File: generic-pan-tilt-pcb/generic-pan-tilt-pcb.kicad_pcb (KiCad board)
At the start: 2 copper layers, 85 x 50 mm, 89 parts, among them J1 B4P-VH-FB-B, J10 USB4115-03-C, J11 Conn_01x08, J12 Conn_01x08, J13 Conn_01x05, J2 NC5MAV, J3 NC5FAV, J4 Conn_01x03, J5 BM03B-SRSS-TB, J6 Conn_01x03, J7 BM03B-SRSS-TB, J8 B12B-PH-SM4-TB, J9 B12B-PH-SM4-TB, SW1 PTS 647 SK70 SMTR2 LFS, SW2 PTS 647 SK70 SMTR2 LFS, SW3 219-12LPST, U1 RP2040, U2 W25Q128JVS, U3 AP63203WU, U4 ISO1450DW, U5 MCP23017_SO, U6 LIS3DH, Y1 ABM8-272-T3

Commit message: layout progress
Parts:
- moved C28 194.8 mm to (162.2, 110.5)
- moved C14 192.4 mm to (158.9, 116.7), turned to 90 degrees
- moved C23 192.0 mm to (120.0, 121.0), turned to 90 degrees
- moved C26 189.2 mm to (128.0, 116.3), turned to -90 degrees
- moved C16 185.4 mm to (153.9, 116.7), turned to 90 degrees
- moved C25 182.6 mm to (125.3, 107.0), turned to 0 degrees
- moved C27 180.3 mm to (125.3, 108.5), turned to 0 degrees
- moved R15 177.6 mm to (183.8, 112.2)
- moved R16 177.6 mm to (183.8, 114.8)
- moved R17 177.6 mm to (183.8, 117.3)
- moved C15 176.2 mm to (159.0, 87.8), turned to 0 degrees
- moved C24 174.7 mm to (122.5, 95.5), turned to -90 degrees
- moved C13 174.6 mm to (156.0, 85.2), turned to 90 degrees
- moved C11 173.4 mm to (159.8, 93.0), turned to 0 degrees
- moved C7 173.4 mm to (150.7, 98.5), turned to -90 degrees
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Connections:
- net Net-(PS1-+Vout) renamed /generic-pan-tilt-pcb_rs485/+3V3_ISO_UNFILTERED
- net Net-(U1-USB_DM) renamed /generic-pan-tilt-pcb_rp2040/USB_UNTERMINATED_D+
- net Net-(U1-USB_DP) renamed /generic-pan-tilt-pcb_rp2040/USB_UNTERMINATED_D-
- net Net-(U3-BST) renamed /generic-pan-tilt-pcb_24v_to_3.3v/+3V3_BST
- net Net-(U3-SW) renamed /generic-pan-tilt-pcb_24v_to_3.3v/+3V3_UNFILTERED
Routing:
- net +3V3: track 0.00 -> 269.7 mm, vias 0 -> 6
- net +24V: track 0.00 -> 103.6 mm
- net /I2C_MOT_SCL: track 0.00 -> 65.5 mm, vias 0 -> 3
- net /I2C_MOT_SDA: track 0.00 -> 65.3 mm, vias 0 -> 3
- net /SPI_MOT_PICO: track 0.00 -> 60.1 mm, vias 0 -> 4
- net /SPI_MOT_POCI: track 0.00 -> 58.2 mm, vias 0 -> 3
- net /SPI_MOT_CS_MOT0_GPIO: track 0.00 -> 58.0 mm, vias 0 -> 2
- net /RS485_B-: track 0.00 -> 57.5 mm
- net /SPI_MOT_SCK: track 0.00 -> 57.0 mm, vias 0 -> 3
- net /SPI_MOT_CS_MOT0_CNTLR: track 0.00 -> 53.9 mm, vias 0 -> 2
- net GND: track 0.00 -> 53.8 mm, vias 0 -> 10
- net /RS485_A+: track 0.00 -> 45.5 mm, vias 0 -> 1
- net /generic-pan-tilt-pcb_dmx-expansion/EXP_IN_+: track 0.00 -> 35.7 mm
- net +1V1: track 0.00 -> 33.6 mm, vias 0 -> 3
- net /RS485_OUT_B-: track 0.00 -> 32.0 mm
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- added copper zone on B.Cu, net /RS485_GND
- added copper zone on F.Cu, net /RS485_GND
- added copper zone on B.Cu, net GND
- added copper zone on F.Cu, net GND
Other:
- outline, holes or cut-outs redrawn

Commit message: more progress
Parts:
- removed J4, J6: Conn_01x03, Connector_PinHeader_2.54mm:PinHeader_1x03_P2.54mm_Vertical_SMD_Pin1Left
- removed R20: 17Ω, Resistor_SMD:R_0603_1608Metric
- C26: value 4.7μF 10V -> 10µF 10V
- C27: value 10µF 10V -> 4.7μF 10V
- D3: value Inolux_IN-P55TATRGB -> LTST-C235KGKRKT; footprint LED_SMD:LED_Inolux_IN-P55TATRGB_PLCC6_5.0x5.5mm_P1.8mm -> LED_SMD:LED_LiteOn_LTST-C235KGKRKT; moved to B.Cu
- J10: moved to B.Cu
- R19: value 8Ω -> 17Ω
- moved C30 131.4 mm to (171.8, 128.2)
- moved C29 125.5 mm to (165.2, 128.0)
- moved U6 115.5 mm to (159.2, 127.8)
- moved R11 77.7 mm to (156.8, 117.0)
- moved R12 75.8 mm to (156.8, 115.5)
- moved U5 60.2 mm to (229.5, 95.5)
- moved D2 57.7 mm to (161.2, 83.0), turned to 0 degrees
- moved R3 56.7 mm to (160.5, 85.2), turned to 90 degrees
- moved D1 56.6 mm to (158.2, 83.0)
- moved R1 56.2 mm to (155.2, 83.0), turned to 0 degrees
- moved J11 53.7 mm to (150.5, 120.0), turned to -90 degrees
- moved R2 48.8 mm to (116.5, 94.8)
- moved R8 44.2 mm to (129.2, 92.2), turned to 0 degrees
- moved SW2 42.9 mm to (124.5, 89.2), turned to 90 degrees
- moved SW1 38.7 mm to (118.5, 89.2), turned to 90 degrees
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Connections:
- D3 pad 1: Net-(D3-KB) -> Net-(D3-K2)
- D3 pad 2: Net-(D3-KR) -> +3V3
- D3 pad 3: Net-(D3-KG) -> +3V3
- D3 pad 4: +3V3 -> Net-(D3-K1)
- R18 pad 1: /generic-pan-tilt-pcb_hid/LED1_G -> /generic-pan-tilt-pcb_hid/LED1_R
- R18 pad 2: Net-(D3-KG) -> Net-(D3-K1)
- R19 pad 1: Net-(D3-KR) -> Net-(D3-K2)
- R19 pad 2: /generic-pan-tilt-pcb_hid/LED1_R -> /generic-pan-tilt-pcb_hid/LED1_G
- U5 pad 3: /generic-pan-tilt-pcb_hid/LED1_B -> unconnected-(U5-GPB2-Pad3)
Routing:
- net +3V3: track 269.7 -> 359.3 mm, vias 6 -> 5
- net /EXP_CS0: track 0.00 -> 71.5 mm, vias 0 -> 3
- net /EXP_IRQ0: track 0.00 -> 56.5 mm, vias 0 -> 1
- net /EXP_IRQ1: track 0.00 -> 55.3 mm, vias 0 -> 1
- net /BOOTSEL: track 16.7 -> 65.8 mm, vias 0 -> 2
- net GND: track 53.8 -> 102.5 mm, vias 10 -> 28
- net /UART_TX: track 0.00 -> 48.3 mm, vias 0 -> 2
- net /EXP_PICO: track 0.00 -> 43.5 mm, vias 0 -> 1
- net /UART_RX: track 0.00 -> 40.4 mm, vias 0 -> 2
- net /I2C0_SCL: track 2.71 -> 41.5 mm
- net /EXP_POCI: track 0.00 -> 37.8 mm, vias 0 -> 1
- net /RESET: track 0.00 -> 35.6 mm
- net /I2C0_SDA: track 2.72 -> 34.3 mm
- net /SWDIO: track 0.00 -> 17.4 mm
- net /SWCLK: track 0.00 -> 14.3 mm
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
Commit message: a very stubborn time feels very accurate
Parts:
- moved U5 61.3 mm to (168.9, 104.8)
- moved FID1 39.7 mm to (177.8, 108.5)
- moved FID2 39.7 mm to (177.8, 111.1)
- moved FID3 39.7 mm to (177.8, 113.6)
- moved FID4 39.7 mm to (177.8, 116.2)
- moved SW3 37.3 mm to (169.9, 102.6)
- moved R4 12.0 mm to (164.4, 76.4)
- moved C12 1.19 mm to (159.0, 92.4), turned to 90 degrees
- moved C11 1.02 mm to (160.6, 92.4), turned to 90 degrees
- moved J10 0.80 mm to (170.1, 78.7)
- moved C7 0.76 mm to (149.6, 99.4)
- moved C6 0.38 mm to (155.3, 97.9)
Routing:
- net /UART_TX: track 48.3 -> 1.54 mm, vias 2 -> 1
- net /UART_RX: track 40.4 -> 1.44 mm, vias 2 -> 1
- net GND: track 102.5 -> 66.9 mm, vias 28 -> 25
- net /EXP_RESET: track 1.41 -> 33.0 mm
- net /EXP_CS1: track 2.18 -> 25.0 mm, vias 1 -> 2
- net /EXP_SCK: track 2.19 -> 18.8 mm
- net +3V3: track 359.3 -> 342.8 mm, vias 5 -> 6
- net /USB_D+: track 16.1 -> 29.2 mm
- net /EXP_PICO: track 43.5 -> 33.0 mm
- net Net-(J10-CC2): track 9.64 -> 0.00 mm
- net /I2C_MOT_SCL: track 67.1 -> 75.4 mm
- net /USB_D-: track 20.6 -> 13.8 mm, vias 2 -> 0
- net +24V: track 101.3 -> 107.8 mm
- net /I2C_MOT_SDA: track 69.0 -> 74.7 mm
- net /SPI_MOT_PICO: track 60.6 -> 56.4 mm, vias 4 -> 3
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
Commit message: make board bigger
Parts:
- moved C23 5.00 mm to (115.0, 121.0)
- moved C25 5.00 mm to (120.3, 107.0)
- moved C26 5.00 mm to (123.0, 116.3)
- moved C27 5.00 mm to (120.3, 108.5)
- moved J13 5.00 mm to (130.4, 120.0)
- moved J2 5.00 mm to (111.0, 103.5)
- moved J3 5.00 mm to (136.4, 103.5)
- moved JP1 5.00 mm to (137.5, 113.5)
- moved JP2 5.00 mm to (130.3, 113.5)
- moved L2 5.00 mm to (125.5, 117.1)
- moved PS1 5.00 mm to (118.0, 121.1)
- moved U4 5.00 mm to (124.1, 99.2)
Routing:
- net +3V3: track 342.8 -> 0.00 mm, vias 6 -> 0
- net +24V: track 107.8 -> 0.00 mm
- net /I2C_MOT_SCL: track 75.4 -> 0.00 mm, vias 3 -> 0
- net /I2C_MOT_SDA: track 74.7 -> 0.00 mm, vias 3 -> 0
- net /EXP_CS0: track 72.0 -> 0.00 mm, vias 3 -> 0
- net GND: track 66.9 -> 0.00 mm, vias 25 -> 0
- net /BOOTSEL: track 66.8 -> 0.00 mm, vias 2 -> 0
- net /SPI_MOT_POCI: track 61.0 -> 0.00 mm, vias 4 -> 0
- net /SPI_MOT_SCK: track 59.6 -> 0.00 mm, vias 3 -> 0
- net /SPI_MOT_CS_MOT0_GPIO: track 57.7 -> 0.00 mm, vias 2 -> 0
- net /EXP_IRQ0: track 57.6 -> 0.00 mm, vias 1 -> 0
- net /RS485_B-: track 57.5 -> 0.00 mm
- net /SPI_MOT_PICO: track 56.4 -> 0.00 mm, vias 3 -> 0
- net /EXP_IRQ1: track 56.0 -> 0.00 mm, vias 1 -> 0
- net /SPI_MOT_CS_MOT0_CNTLR: track 53.2 -> 0.00 mm, vias 2 -> 0
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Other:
- board size 85 x 50 mm -> 115 x 57 mm

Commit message: begin new routing
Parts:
- C1, C10, C11, C12, C13, C14, C15, C16, C17, C18, C19, C2, C20, C21, C22, C23, C24, C25, C26, C27, C28, C29, C3, C30, C4, C5, C6, C7, C8, C9: footprint Capacitor_SMD:C_0603_1608Metric -> Capacitor_SMD:C_0402_1005Metric
- J11, J12: moved to F.Cu
- R1, R10, R11, R12, R13, R14, R15, R16, R17, R18, R19, R2, R3, R4, R5, R6, R7, R8, R9: footprint Resistor_SMD:R_0603_1608Metric -> Capacitor_SMD:C_0402_1005Metric
- moved J9 62.8 mm to (86.0, 88.2), turned to 90 degrees
- moved J11 56.8 mm to (124.0, 69.8), turned to 90 degrees
- moved C17 32.8 mm to (84.0, 117.0), turned to 90 degrees
- moved U3 31.2 mm to (86.5, 115.9), turned to 90 degrees
- moved C18 30.9 mm to (88.8, 114.8), turned to 90 degrees
- moved J12 30.0 mm to (164.0, 69.8), turned to -90 degrees
- moved J1 29.5 mm to (93.5, 107.0)
- moved C19 28.7 mm to (84.0, 114.3), turned to -90 degrees
- moved C20 28.7 mm to (82.5, 114.3), turned to -90 degrees
- moved J8 25.5 mm to (94.5, 88.2), turned to 90 degrees
- moved C22 24.5 mm to (82.5, 111.3), turned to 90 degrees
- moved C21 24.4 mm to (84.0, 111.2), turned to 90 degrees
- moved L1 24.1 mm to (88.0, 110.4), turned to 90 degrees
- moved H2 8.06 mm to (182.0, 69.5)
- moved H1 7.00 mm to (99.0, 69.5)
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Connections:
- net Net-(C2-Pad2) renamed /generic-pan-tilt-pcb_rp2040/XOUT_R
- net Net-(U1-XIN) renamed /generic-pan-tilt-pcb_rp2040/XIN
- net Net-(U1-XOUT) renamed /generic-pan-tilt-pcb_rp2040/XOUT
- J11 pad 1: +3V3 -> GND
- J11 pad 2: /EXP_SCK -> /EXP_RESET
- J11 pad 3: /EXP_PICO -> /I2C0_SCL
- J11 pad 4: /EXP_POCI -> /I2C0_SDA
- J11 pad 5: /I2C0_SDA -> /EXP_POCI
- J11 pad 6: /I2C0_SCL -> /EXP_PICO
- J11 pad 7: /EXP_RESET -> /EXP_SCK
- J11 pad 8: GND -> +3V3
- J12 pad 1: +3V3 -> GND
- J12 pad 2: /EXP_CS0 -> unconnected-(J12-Pin_2-Pad2)
- J12 pad 3: /EXP_CS1 -> unconnected-(J12-Pin_3-Pad3)
- J12 pad 4: /EXP_IRQ0 -> /EXP_IRQ1
- J12 pad 5: /EXP_IRQ1 -> /EXP_IRQ0
- J12 pad 6: unconnected-(J12-Pin_6-Pad6) -> /EXP_CS1
- J12 pad 7: unconnected-(J12-Pin_7-Pad7) -> /EXP_CS0
- J12 pad 8: GND -> +3V3
- J13 pad 1: /generic-pan-tilt-pcb_dmx-expansion/EXP_IN_+ -> /RS485_GND
- J13 pad 2: /generic-pan-tilt-pcb_dmx-expansion/EXP_IN_- -> /generic-pan-tilt-pcb_dmx-expansion/EXP_OUT_+
- J13 pad 4: /generic-pan-tilt-pcb_dmx-expansion/EXP_OUT_+ -> /generic-pan-tilt-pcb_dmx-expansion/EXP_IN_-
- J13 pad 5: /RS485_GND -> /generic-pan-tilt-pcb_dmx-expansion/EXP_IN_+
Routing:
- net +3V3: track 0.00 -> 67.8 mm
- net +24V: track 0.00 -> 49.0 mm, vias 0 -> 1
- net /generic-pan-tilt-pcb_rs485/+3V3_ISO: track 0.00 -> 16.7 mm
- net /SPI_MOT_SCK: track 0.00 -> 8.50 mm
- net /SPI_MOT_POCI: track 0.00 -> 8.50 mm
- net /SPI_MOT_PICO: track 0.00 -> 8.50 mm
- net /I2C_MOT_SDA: track 0.00 -> 8.50 mm
- net /I2C_MOT_SCL: track 0.00 -> 8.50 mm
- net GND: track 0.00 -> 3.54 mm, vias 0 -> 35
- net /generic-pan-tilt-pcb_rs485/+3V3_ISO_UNFILTERED: track 0.00 -> 2.63 mm
- net /RS485_GND: track 0.00 -> 0.06 mm, vias 0 -> 4
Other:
- board size 115 x 57 mm -> 104 x 57 mm

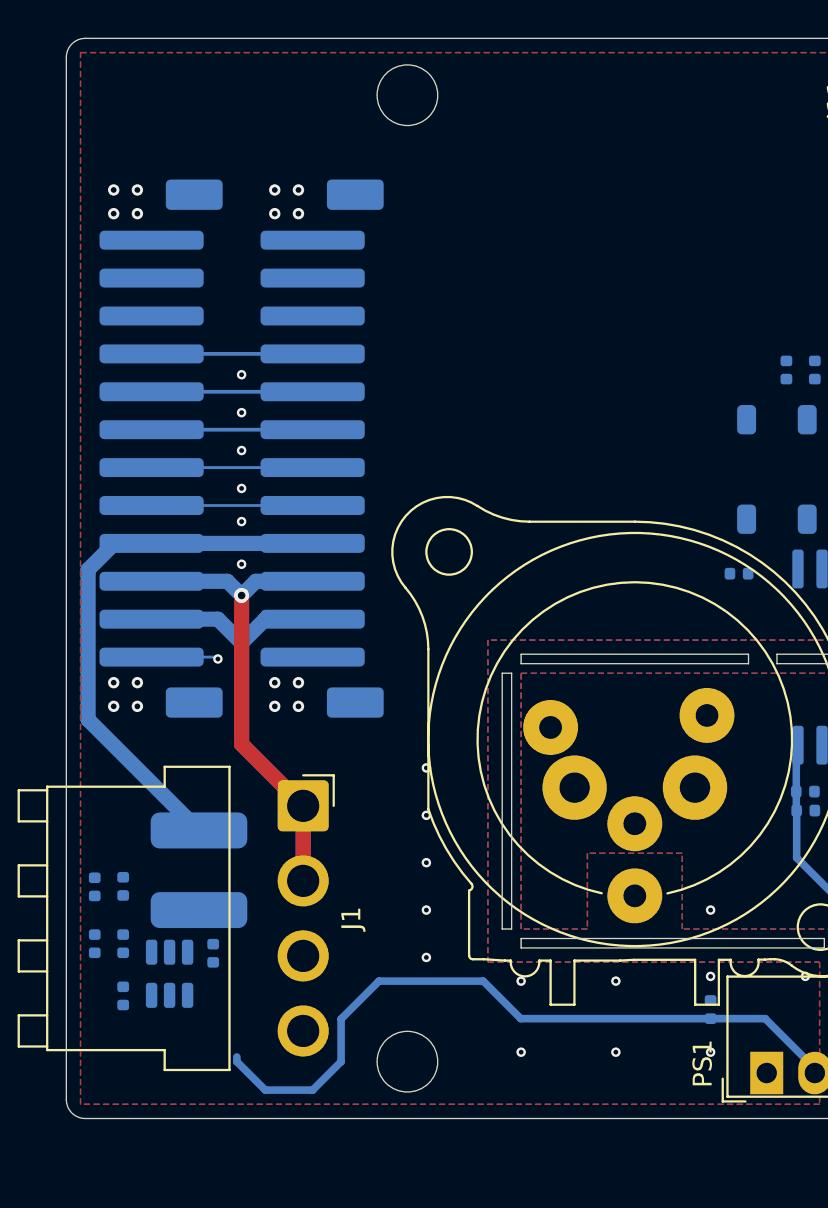
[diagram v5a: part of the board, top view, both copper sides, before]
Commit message: more pcb, kicost maf digikey mouser
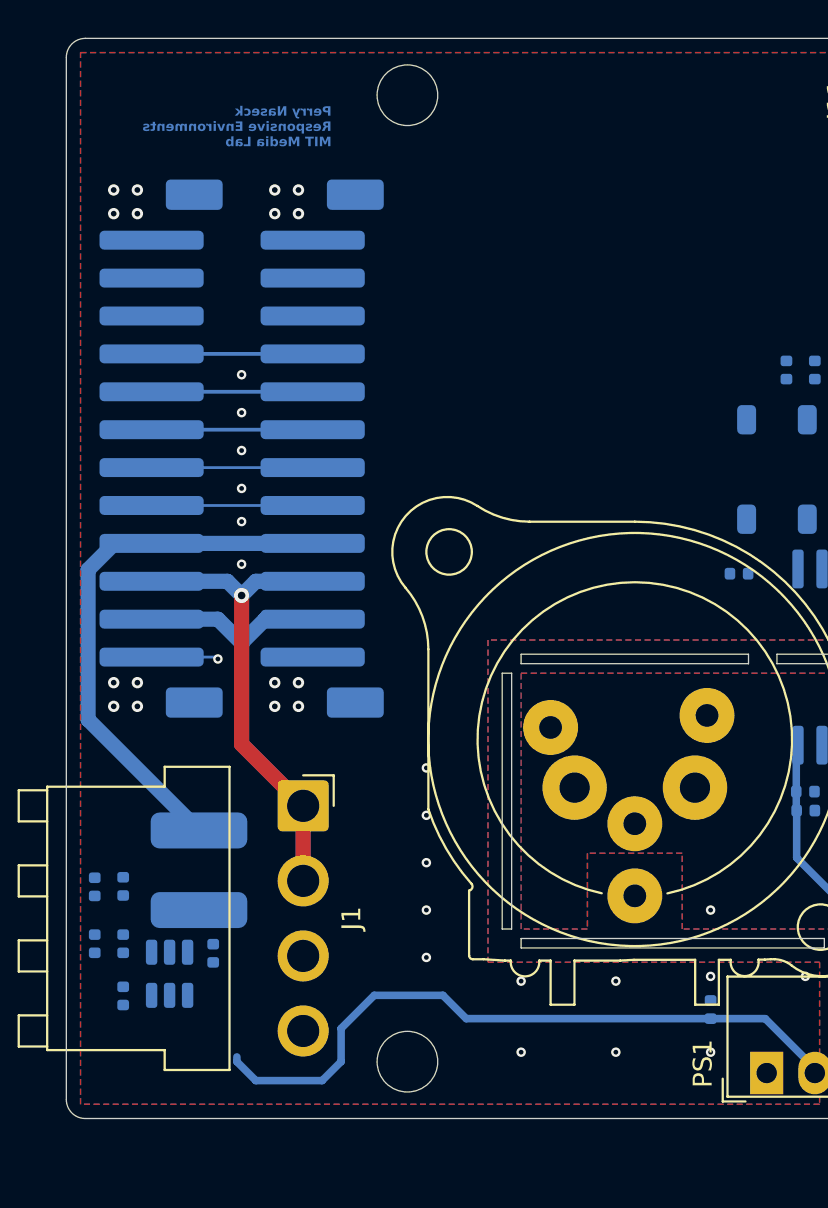
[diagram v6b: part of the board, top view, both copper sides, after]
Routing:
- net +3V3: track 67.8 -> 66.5 mm
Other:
- board text added: "Perry Naseck Responsive Environments MIT Media Lab"
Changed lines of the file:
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@@
 		(layer "Edge.Cuts")
+	)
+	(gr_text "Perry Naseck\nResponsive Environments\nMIT Media Lab"
+		(at 95 72.25 0)
+		(layer "B.Cu")
+		(effects
+			(font
+				(size 0.5 0.5)
+				(thickness 0.125)
+				(bold yes)
+			)
+			(justify left bottom mirror)
+		)
 	)
 	(dimension
@@
 	)
 	(segment
-		(start 91.5 122)
-		(end 94 122)
+		(start 94.5 121.5)
+		(end 95.5 120.5)
 		(width 0.4)
 		(layer "B.Cu")
@@
 		(start 115 118.23)
 		(end 117.88 118.23)
-		(width 0.4)
-		(layer "B.Cu")
-		(net 3)
-	)
-	(segment
-		(start 90 120.5)
-		(end 91.5 122)
 		(width 0.4)
 		(layer "B.Cu")
@@
 	)
 	(segment
+		(start 102.105 118.23)
+		(end 115 118.23)
+		(width 0.4)
+		(layer "B.Cu")
+		(net 3)
+	)
+	(segment
+		(start 91 121.5)
+		(end 94.5 121.5)
+		(width 0.4)
+		(layer "B.Cu")
+		(net 3)
+	)
+	(segment
+		(start 90 120.5)
+		(end 91 121.5)
+		(width 0.4)
+		(layer "B.Cu")
+		(net 3)
+	)
+	(segment
+		(start 90 120.25)
+		(end 90 120.5)
+		(width 0.4)
+		(layer "B.Cu")
+		(net 3)
+	)
+	(segment
 		(start 85.5 93.15)
 		(end 83.54099 93.15)
@@
 	)
 	(segment
-		(start 95.5 120.5)
-		(end 95.5 118.25)
-		(width 0.4)
-		(layer "B.Cu")
-		(net 3)
-	)
-	(segment
 		(start 120.5 120.85)
 		(end 120.5 121.1)
-		(width 0.4)
-		(layer "B.Cu")
-		(net 3)
-	)
-	(segment
-		(start 104.98 118.23)
-		(end 115 118.23)
 		(width 0.4)
 		(layer "B.Cu")
@@
 	)
 	(segment
-		(start 94 122)
-		(end 95.5 120.5)
-		(width 0.4)
-		(layer "B.Cu")
-		(net 3)
-	)
-	(segment
-		(start 97.5 116.25)
-		(end 103 116.25)
-		(width 0.4)
-		(layer "B.Cu")
-		(net 3)
-	)
-	(segment
 		(start 117.88 118.23)
 		(end 120.5 120.85)
-		(width 0.4)
-		(layer "B.Cu")
-		(net 3)
-	)
-	(segment
-		(start 90 120.25)
-		(end 90 120.5)
-		(width 0.4)
-		(layer "B.Cu")
-		(net 3)
-	)
-	(segment
-		(start 103 116.25)
-		(end 104.98 118.23)
 		(width 0.4)
 		(layer "B.Cu")
@@
 	)
 	(segment
+		(start 95.5 118.75)
+		(end 97.25 117)
+		(width 0.4)
+		(layer "B.Cu")
+		(net 3)
+	)
+	(segment
 		(start 83.54099 93.15)
 		(end 82.15 94.54099)
@@
 	)
 	(segment
-		(start 95.5 118.25)
-		(end 97.5 116.25)
-		(width 0.4)
-		(layer "B.Cu")
+		(start 100.875 117)
+		(end 102.105 118.23)
+		(width 0.4)
+		(layer "B.Cu")
+		(net 3)
+	)
+	(segment
+		(start 97.25 117)
+		(end 100.875 117)
+		(width 0.4)
+		(layer "B.Cu")
+		(net 3)
+	)
+	(segment
+		(start 95.5 120.5)
+		(end 95.5 118.75)
+		(width 0.4)
+		(layer "B.Cu")
